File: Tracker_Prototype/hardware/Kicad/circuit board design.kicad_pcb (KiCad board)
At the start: 2 copper layers, 31 x 17.8 mm, 23 parts, among them J1 Conn_01x06, J2 GND, J3 3.3V, U1 MAX-M8C, U3 CMWX1ZZABZ-078, U6 MS5607-02BA

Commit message: Fully routed the board
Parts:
- removed C2: 10uF, Capacitor_SMD:C_0603_1608Metric
- removed C3: 100nF, Capacitor_SMD:C_0402_1005Metric
- added No connection: Unconnected, Connector_Wire:SolderWirePad_1x01_Drill0.8mm, F.Cu at (296.0, 170.1)
- added R1: 100K, Resistor_SMD:R_0402_1005Metric, F.Cu at (281.3, 161.7)
- added R2: 100K, Resistor_SMD:R_0402_1005Metric, F.Cu at (281.3, 163.3)
- 3.3V: renamed from J3; footprint Connector_PinHeader_1.00mm:PinHeader_1x01_P1.00mm_Vertical -> Connector_Wire:SolderWirePad_1x01_Drill0.8mm
- AE1, AE2: footprint Connector_PinHeader_1.00mm:PinHeader_1x01_P1.00mm_Vertical -> Connector_Wire:SolderWirePad_1x01_Drill0.8mm
- GND: renamed from J2; footprint Connector_PinHeader_1.00mm:PinHeader_1x01_P1.00mm_Vertical -> Connector_Wire:SolderWirePad_1x01_Drill0.8mm
- U6: moved to F.Cu
- moved C14 47.5 mm to (292.0, 162.8), turned to 270 degrees
- moved R4 35.6 mm to (283.2, 161.7), turned to 180 degrees
- moved C1 34.0 mm to (272.1, 163.8), turned to 180 degrees
- moved R5 31.7 mm to (283.2, 163.3)
- moved R3 26.8 mm to (268.4, 171.5), turned to 270 degrees
- moved C5 21.1 mm to (274.6, 178.6)
- moved C10 20.5 mm to (272.2, 178.6), turned to 180 degrees
- moved C7 18.9 mm to (277.1, 178.6)
- moved C13 15.3 mm to (288.3, 178.1), turned to 180 degrees
- moved U6 15.1 mm to (288.3, 162.9)
- moved C12 15.0 mm to (291.4, 178.1), turned to 180 degrees
- moved J1 2.03 mm to (268.7, 178.1)
- moved U1 2.03 mm to (288.7, 171.2)
- moved 3.3V 1.80 mm to (296.0, 173.1)
- moved C9 1.20 mm to (273.4, 162.2), turned to 270 degrees
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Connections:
- J1 pad 6: (no net) -> Net-(J1-Pad6)
- U1 pad 14: (no net) -> Net-(U1-Pad14)
- U1 pad 15: (no net) -> Net-(U1-Pad15)
- U1 pad 2: (no net) -> Net-(U1-Pad2)
- U1 pad 3: (no net) -> Net-(U1-Pad3)
- U3 pad 1: (no net) -> /VDD_TCXO
- U3 pad 10: (no net) -> Net-(U3-Pad10)
- U3 pad 11: (no net) -> Net-(U3-Pad11)
- U3 pad 12: (no net) -> Net-(U3-Pad12)
- U3 pad 13: (no net) -> Net-(U3-Pad13)
- U3 pad 14: /VDD_TCXO -> Net-(U3-Pad14)
- U3 pad 18: (no net) -> Net-(U3-Pad18)
- U3 pad 19: (no net) -> Net-(U3-Pad19)
- U3 pad 2: (no net) -> Net-(U3-Pad2)
- U3 pad 20: (no net) -> Net-(U3-Pad20)
- U3 pad 21: (no net) -> Net-(U3-Pad21)
- U3 pad 22: (no net) -> Net-(U3-Pad22)
- U3 pad 23: (no net) -> Net-(U3-Pad23)
- U3 pad 24: (no net) -> /V_SOLAR
- U3 pad 28: (no net) -> Net-(U3-Pad28)
- U3 pad 29: (no net) -> Net-(U3-Pad29)
- U3 pad 30: (no net) -> Net-(U3-Pad30)
- U3 pad 31: (no net) -> Net-(U3-Pad31)
- U3 pad 32: (no net) -> Net-(U3-Pad32)
- U3 pad 33: (no net) -> Net-(U3-Pad33)
- U3 pad 37: (no net) -> Net-(U3-Pad37)
- U3 pad 38: (no net) -> Net-(U3-Pad38)
- U3 pad 39: (no net) -> Net-(U3-Pad39)
- U3 pad 40: (no net) -> Net-(U3-Pad40)
- U3 pad 45: (no net) -> Net-(U3-Pad45)
- U3 pad 46: (no net) -> Net-(U3-Pad46)
- U3 pad 47: (no net) -> Net-(U3-Pad47)
- U3 pad 8: (no net) -> Net-(U3-Pad8)
- U3 pad 9: (no net) -> Net-(U3-Pad9)
- U6 pad 6: (no net) -> Net-(U6-Pad6)
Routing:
- net +3V3: track 0.00 -> 76.2 mm, vias 0 -> 2
- net GND: track 0.00 -> 52.5 mm, vias 0 -> 8
- net /I2C1_SDA: track 0.00 -> 32.2 mm, vias 0 -> 3
- net /I2C1_SCL: track 0.00 -> 26.8 mm, vias 0 -> 2
- net /RESET: track 0.00 -> 19.2 mm, vias 0 -> 1
- net /SWDIO: track 0.00 -> 11.9 mm, vias 0 -> 1
- net /GPS_EXTINT: track 0.00 -> 10.0 mm
- net /GPS_TIMEPULSE: track 0.00 -> 8.59 mm
- net /SWCLK: track 0.00 -> 8.57 mm, vias 0 -> 1
- net Net-(C9-Pad1): track 0.00 -> 8.43 mm
- net /GPS_SAFEBOOT: track 0.00 -> 7.46 mm
- net Net-(AE2-Pad1): track 0.00 -> 6.14 mm
- net /V_SOLAR: track 0.00 -> 4.84 mm
- net Net-(AE1-Pad1): track 0.00 -> 3.27 mm
- net Net-(R3-Pad1): track 0.00 -> 1.96 mm
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- added copper zone on B.Cu, net GND
- added copper zone on F.Cu, net GND
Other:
- board size 31 x 17.8 mm -> 31 x 20.1 mm
- net class FETs removed
- net class Power: trace_width 2 -> 0.5
- net class sense removed

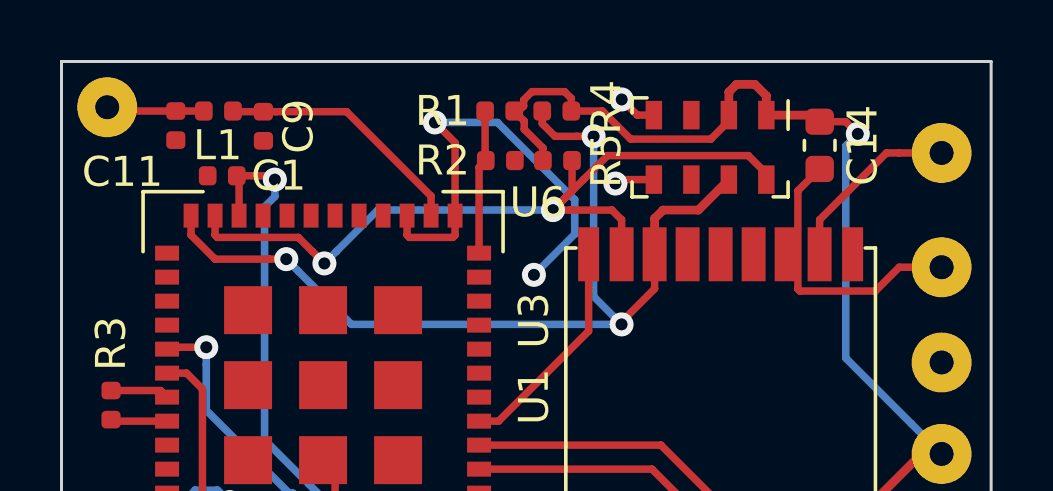
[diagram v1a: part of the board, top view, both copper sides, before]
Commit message: Changed the TCXO power pin. Changed the track width for RF transmission lines to 0.86mm
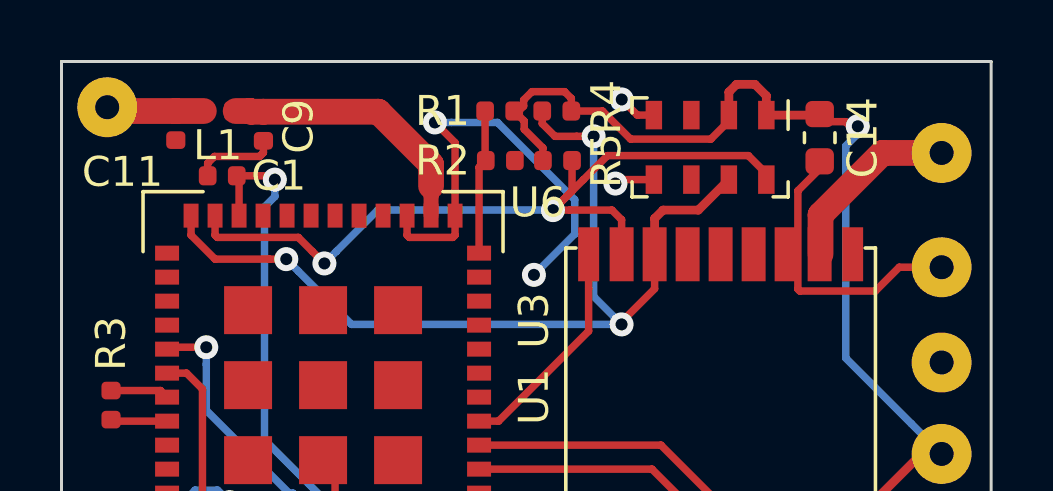
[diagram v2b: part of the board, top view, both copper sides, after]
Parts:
- moved C14 0.25 mm to (292.0, 162.6)
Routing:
- net GND: track 52.5 -> 55.3 mm
- net Net-(C9-Pad1): track 8.43 -> 8.96 mm
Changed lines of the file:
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@@
 (kicad_pcb (version 20171130) (host pcbnew "(5.1.2)-1")
   (general
-    (thickness 1.6)
+    (thickness 0.6)
     (drawings 7)
-    (tracks 228)
+    (tracks 234)
     (zones 0)
     (modules 24)
@@
   )
   (layers
-    (0 F.Cu signal hide)
+    (0 F.Cu signal)
     (31 B.Cu signal)
     (32 B.Adhes user hide)
     (33 F.Adhes user)
     (34 B.Paste user hide)
-    (35 F.Paste user)
+    (35 F.Paste user hide)
     (36 B.SilkS user)
     (37 F.SilkS user)
@@
     (last_trace_width 0.25)
     (user_trace_width 0.2)
-    (user_trace_width 0.25)
     (user_trace_width 0.2933)
-    (user_trace_width 0.4)
-    (user_trace_width 2)
+    (user_trace_width 0.5)
+    (user_trace_width 0.8)
+    (user_trace_width 0.86)
+    (user_trace_width 1.08)
     (user_trace_width 2.54)
-    (user_trace_width 5)
     (trace_clearance 0.2)
     (zone_clearance 0.508)
@@
   )
   (module Capacitor_SMD:C_0603_1608Metric (layer F.Cu)
-    (at 291.973 162.814 270)
+    (at 291.973 162.56 270)
     (descr "Capacitor SMD 0603 (1608 Metric), square (rectangular) end terminal, IPC_7351 nominal, (Body size source: http://www.tortai-tech.com/upload/download/2011102023233369053.pdf), generated with kicad-footprint-generator")
     (tags capacitor)
@@
   (segment (start 283.808001 165.771999) (end 283.808001 164.624999) (width 0.25) (layer B.Cu) (net 1))
   (segment (start 282.448 167.132) (end 283.808001 165.771999) (width 0.25) (layer B.Cu) (net 1))
+  (segment (start 271.572 163.41) (end 271.572 163.83) (width 0.25) (layer F.Cu) (net 1))
+  (segment (start 271.79701 163.18499) (end 271.572 163.41) (width 0.25) (layer F.Cu) (net 1))
+  (segment (start 273.30501 163.18499) (end 271.79701 163.18499) (width 0.25) (layer F.Cu) (net 1))
+  (segment (start 273.431 163.059) (end 273.30501 163.18499) (width 0.25) (layer F.Cu) (net 1))
+  (segment (start 273.431 162.664) (end 273.431 163.059) (width 0.25) (layer F.Cu) (net 1))
   (segment (start 272.974 178.562) (end 273.419 178.117) (width 0.25) (layer F.Cu) (net 2))
   (segment (start 273.419 177.431) (end 273.419 176.458) (width 0.25) (layer F.Cu) (net 2))
@@
   (segment (start 288.945 161.807) (end 288.945 162.007) (width 0.25) (layer F.Cu) (net 2))
   (segment (start 288.945 162.007) (end 288.344999 162.607001) (width 0.25) (layer F.Cu) (net 2))
-  (via (at 293.243 162.433) (size 0.8) (drill 0.4) (layers F.Cu B.Cu) (net 2))
+  (via (at 293.243 162.179) (size 0.8) (drill 0.4) (layers F.Cu B.Cu) (net 2))
   (segment (start 291.973 162.0265) (end 292.8365 162.0265) (width 0.25) (layer F.Cu) (net 2))
   (segment (start 292.8365 162.0265) (end 293.243 162.433) (width 0.25) (layer F.Cu) (net 2))
@@
   (segment (start 292.843001 162.832999) (end 292.843001 169.907001) (width 0.25) (layer B.Cu) (net 2))
   (segment (start 293.243 162.433) (end 292.843001 162.832999) (width 0.25) (layer B.Cu) (net 2))
-  (segment (start 273.851 161.694) (end 273.431 161.694) (width 0.25) (layer F.Cu) (net 3))
-  (segment (start 276.205 161.694) (end 273.851 161.694) (width 0.25) (layer F.Cu) (net 3))
-  (segment (start 279.019 164.508) (end 276.205 161.694) (width 0.25) (layer F.Cu) (net 3))
-  (segment (start 279.019 165.158) (end 279.019 164.508) (width 0.25) (layer F.Cu) (net 3))
-  (segment (start 272.438 161.694) (end 272.415 161.671) (width 0.25) (layer F.Cu) (net 3))
-  (segment (start 273.431 161.694) (end 272.438 161.694) (width 0.25) (layer F.Cu) (net 3))
+  (segment (start 279.019 163.449402) (end 279.019 164.173998) (width 0.86) (layer F.Cu) (net 3))
+  (segment (start 273.431 161.694) (end 277.263598 161.694) (width 0.86) (layer F.Cu) (net 3))
+  (segment (start 277.263598 161.694) (end 279.019 163.449402) (width 0.86) (layer F.Cu) (net 3))
+  (segment (start 279.019 164.497998) (end 279.019 164.173998) (width 0.5) (layer F.Cu) (net 3))
+  (segment (start 279.019 165.158) (end 279.019 164.497998) (width 0.5) (layer F.Cu) (net 3))
+  (segment (start 272.988 161.671) (end 272.50501 161.671) (width 0.86) (layer F.Cu) (net 3))
+  (segment (start 273.431 161.694) (end 273.011 161.694) (width 0.86) (layer F.Cu) (net 3))
+  (segment (start 273.011 161.694) (end 272.988 161.671) (width 0.86) (layer F.Cu) (net 3))
   (segment (start 286.471 165.2527) (end 286.471 166.446) (width 0.2933) (layer F.Cu) (net 4))
   (segment (start 286.7507 164.973) (end 286.471 165.2527) (width 0.2933) (layer F.Cu) (net 4))
@@
   (segment (start 290.195 163.957) (end 290.195 163.757) (width 0.25) (layer F.Cu) (net 5))
   (segment (start 290.195 163.757) (end 289.594999 163.156999) (width 0.25) (layer F.Cu) (net 5))
-  (segment (start 294.623508 163.068) (end 296.037 163.068) (width 0.25) (layer F.Cu) (net 6))
-  (segment (start 294.199 163.068) (end 294.623508 163.068) (width 0.25) (layer F.Cu) (net 6))
-  (segment (start 291.971 165.296) (end 294.199 163.068) (width 0.25) (layer F.Cu) (net 6))
-  (segment (start 291.971 166.446) (end 291.971 165.296) (width 0.25) (layer F.Cu) (net 6))
+  (segment (start 292.001009 165.131989) (end 292.001009 166.446) (width 0.86) (layer F.Cu) (net 6))
+  (segment (start 296.037 163.068) (end 294.064998 163.068) (width 0.86) (layer F.Cu) (net 6))
+  (segment (start 294.064998 163.068) (end 292.001009 165.131989) (width 0.86) (layer F.Cu) (net 6))
   (via (at 271.526 169.545) (size 0.8) (drill 0.4) (layers F.Cu B.Cu) (net 7))
   (segment (start 270.282 169.545) (end 270.219 169.608) (width 0.25) (layer F.Cu) (net 7))
@@
   (segment (start 281.269 172.008) (end 284.271 169.006) (width 0.25) (layer F.Cu) (net 14))
   (segment (start 280.619 172.008) (end 281.269 172.008) (width 0.25) (layer F.Cu) (net 14))
-  (segment (start 271.445 161.671) (end 270.51 161.671) (width 0.25) (layer F.Cu) (net 15))
-  (segment (start 268.351 161.671) (end 268.224 161.544) (width 0.25) (layer F.Cu) (net 15))
-  (segment (start 270.51 161.671) (end 268.351 161.671) (width 0.25) (layer F.Cu) (net 15))
+  (segment (start 268.351 161.671) (end 268.224 161.544) (width 0.86) (layer F.Cu) (net 15))
+  (segment (start 270.51 161.671) (end 268.351 161.671) (width 0.86) (layer F.Cu) (net 15))
+  (segment (start 271.445 161.671) (end 270.51 161.671) (width 0.86) (layer F.Cu) (net 15))
   (segment (start 280.619 163.546) (end 280.843 163.322) (width 0.25) (layer F.Cu) (net 16))
   (segment (start 280.619 166.408) (end 280.619 163.546) (width 0.25) (layer F.Cu) (net 16))

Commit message: added in indicator LED, added in push button to circuit only.
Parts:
- added D1: LED, LED_SMD:LED_0402_1005Metric, F.Cu at (267.8, 168.7)
- added R6: R, Resistor_SMD:R_0402_1005Metric, F.Cu at (268.9, 168.7)
- added R7: 100K, Resistor_SMD:R_0402_1005Metric, F.Cu at (293.6, 178.6)
- J4: renamed from No connection
- renumbered GND to J2, 3.3V to J3
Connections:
- U3 pad 1: /VDD_TCXO -> Net-(U3-Pad1)
- U3 pad 14: Net-(U3-Pad14) -> /SWITCH
- U3 pad 39: Net-(U3-Pad39) -> /VDD_TCXO
- U3 pad 40: Net-(U3-Pad40) -> /LED
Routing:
- net /VDD_TCXO: track 1.58 -> 0.00 mm
- net /LED: track 0.00 -> 1.50 mm
- net Net-(D1-Pad2): track 0.00 -> 1.02 mm
- net /SWCLK: track 8.57 -> 9.09 mm
- net GND: track 55.3 -> 55.2 mm, vias 8 -> 7
- net (no net): vias 0 -> 1
